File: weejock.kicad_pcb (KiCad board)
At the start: 2 copper layers, 95.4 x 89.7 mm, 44 parts, among them J2 JST-PH2, K1 PG1350, K10 PG1350, K11 PG1350, K12 PG1350, K13 PG1350, K14 PG1350, K15 PG1350, K16 PG1350, K17 PG1350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

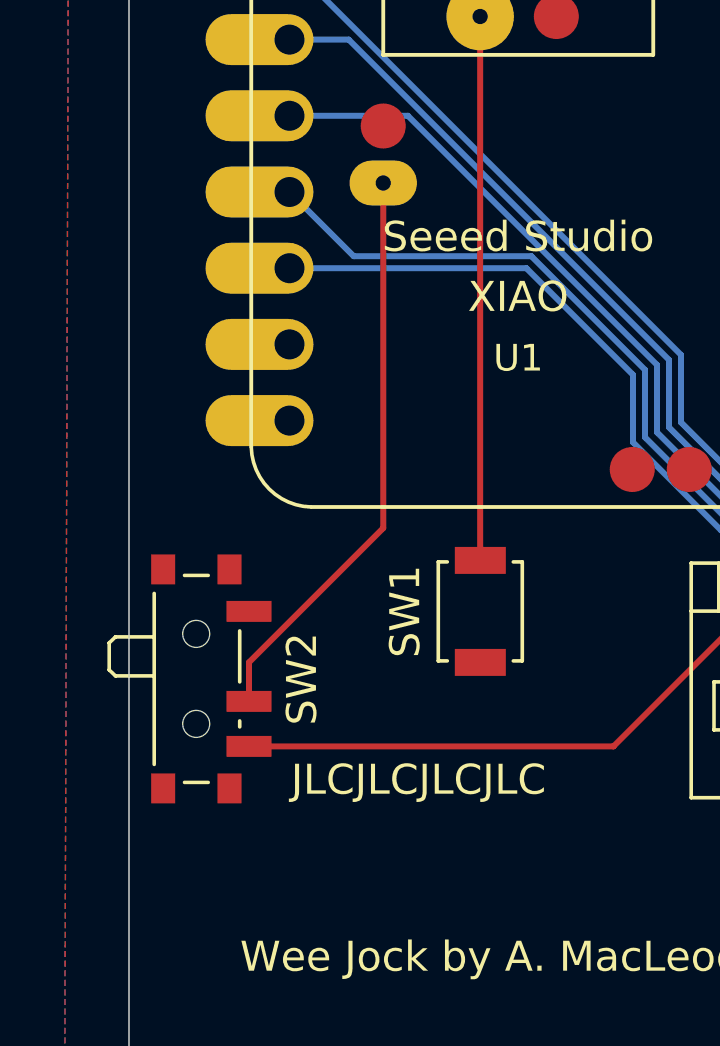
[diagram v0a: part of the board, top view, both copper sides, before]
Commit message: Neatening power switch and adding ON/OFF labels.
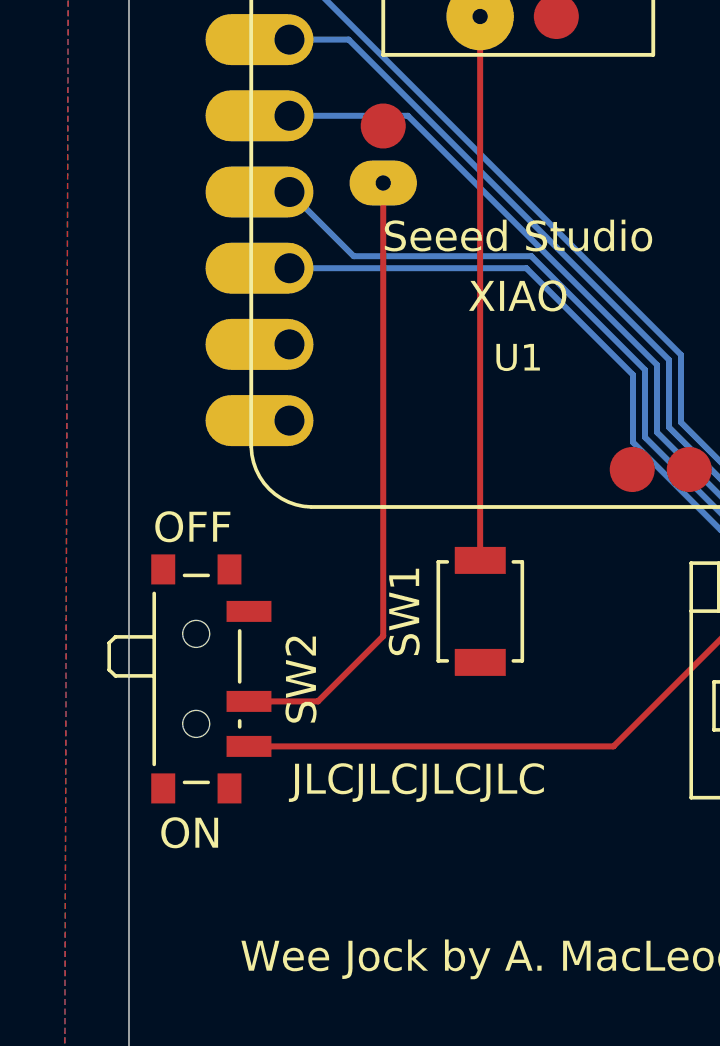
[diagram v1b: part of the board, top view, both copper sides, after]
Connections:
- net Net-(J2-Pin_1) renamed /B+ Supply
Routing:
- net BAT+: track 19.1 -> 20.5 mm
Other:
- board text added: "OFF"
- board text added: "ON"

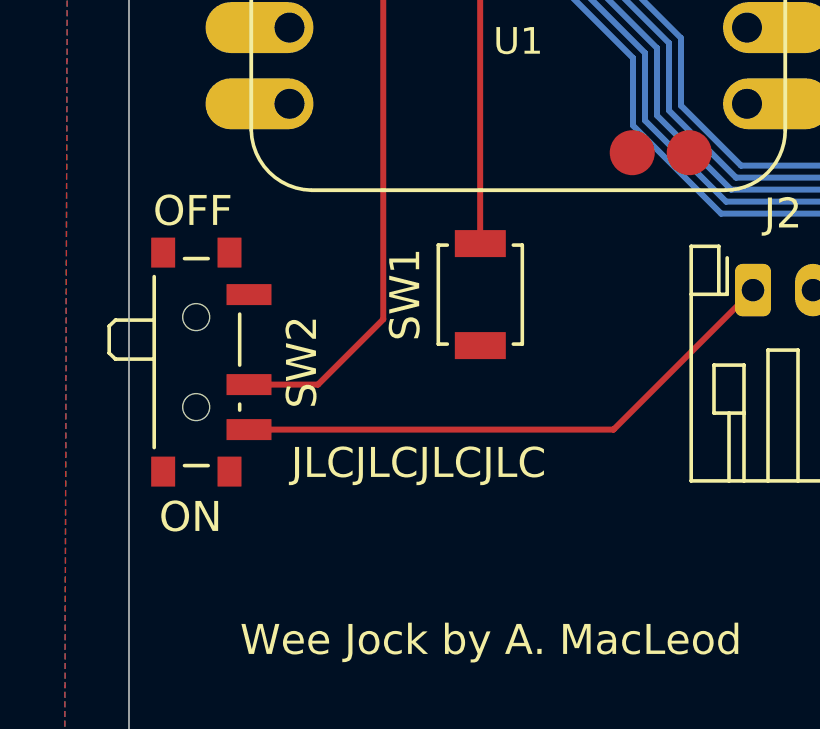
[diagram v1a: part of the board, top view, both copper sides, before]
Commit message: Labeling reset button.
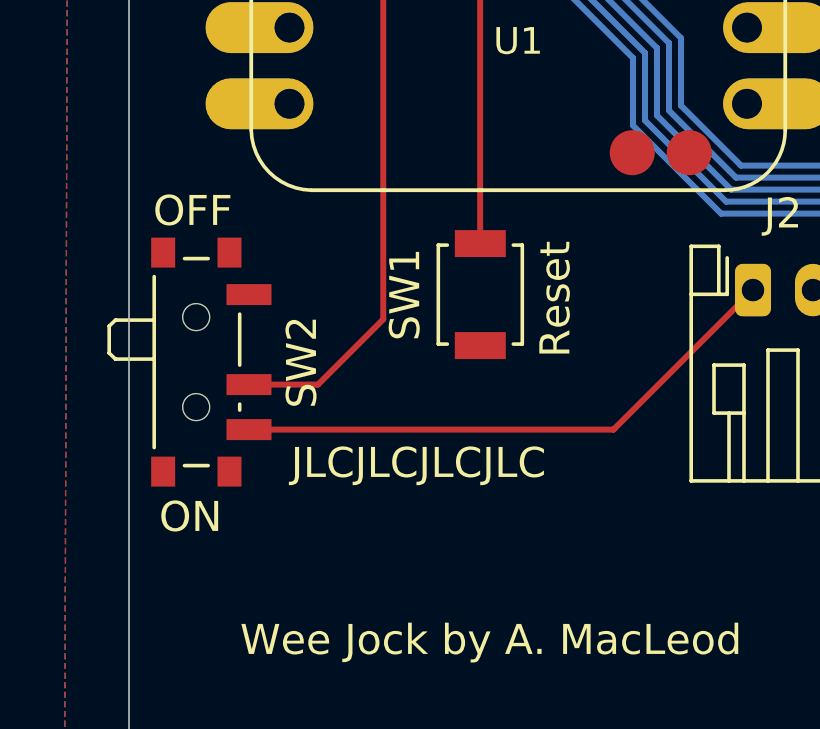
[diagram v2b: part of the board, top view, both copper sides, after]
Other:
- board text added: "Reset"
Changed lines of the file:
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@@
 		(layer "Edge.Cuts")
+	)
+	(gr_text "Reset"
+		(at 89.4 75.4 90)
+		(layer "F.SilkS")
+		(effects
+			(font
+				(size 1 1)
+				(thickness 0.15)
+			)
+			(justify left bottom)
+		)
 	)
 	(gr_text "ON"
@@
 			(font
 				(size 1 1)
-				(thickness 0.1)
+				(thickness 0.15)
 			)
 			(justify left bottom)
@@
 			(font
 				(size 1 1)
-				(thickness 0.1)
+				(thickness 0.15)
 			)
 			(justify left bottom)
